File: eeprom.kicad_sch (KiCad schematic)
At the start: 5 parts, among them U9 24LC02BT-I-SN

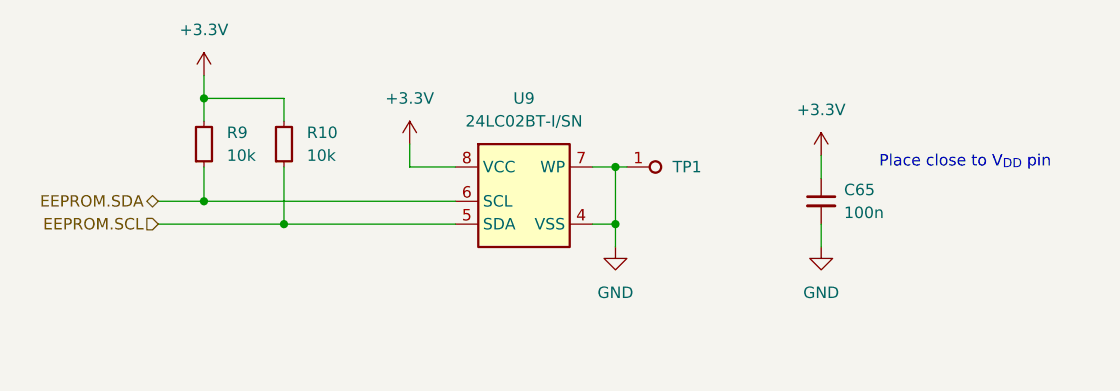
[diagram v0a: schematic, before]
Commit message: [#100650] Change EEPROM memory IC
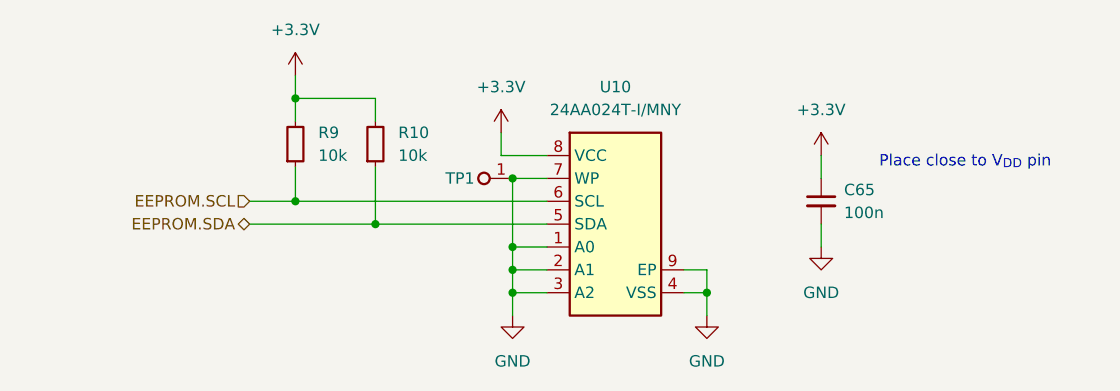
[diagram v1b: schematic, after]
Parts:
- removed U9: 24LC02BT-I-SN, antmicro-footprints:SOIC-8_3.9x4.9x1.75mm_P1.27mm, symbol antmicroMemory:24LC02BT-I-SN
- added U10: 24AA024_TDFN, antmicro-footprints:TDFN-8-1EP_2x3x0.8mm_P0.5mm_EP1.3x1.4mm, symbol antmicroMemory:24AA024_TDFN
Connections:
- net +3.3V: now also U10.8 (VCC)
- net EEPROM.SCL: now also R9.1, U10.6 (SCL); no longer R10.1
- net EEPROM.SDA: now also R10.1, U10.5 (SDA); no longer R9.1
- net GND: now also U10.1 (A0), U10.2 (A1), U10.3 (A2), U10.4 (VSS), U10.7 (WP), U10.9 (EP)
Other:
- moved on the sheet: R10, R9, TP1

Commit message: [#100919] Add test points
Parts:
- added TP4: TP_1mm_SMD, antmicro-footprints:TP_SMD_1mm, symbol antmicroTestPoints:TP_1mm_SMD
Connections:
- net EEPROM.SCL: now also TP1.1
- net EEPROM.SDA: now also TP4.1
- net GND: no longer TP1.1
